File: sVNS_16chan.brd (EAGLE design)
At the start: 51 x 26.4 mm, 56 parts, among them IC2 OPA990IDCKR, IC3 EFM8SB10F8A-A-QFN24EFM8SB10F8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, J1 M50-3631042, J2 M50-3631042, J3 M50-3631042, U1 NT3H2211W0FHKH, U2 LT8410EDC-1#TRMPBF, U3 MUX36S16IRSNR, U4 MUX36S16IRSNR

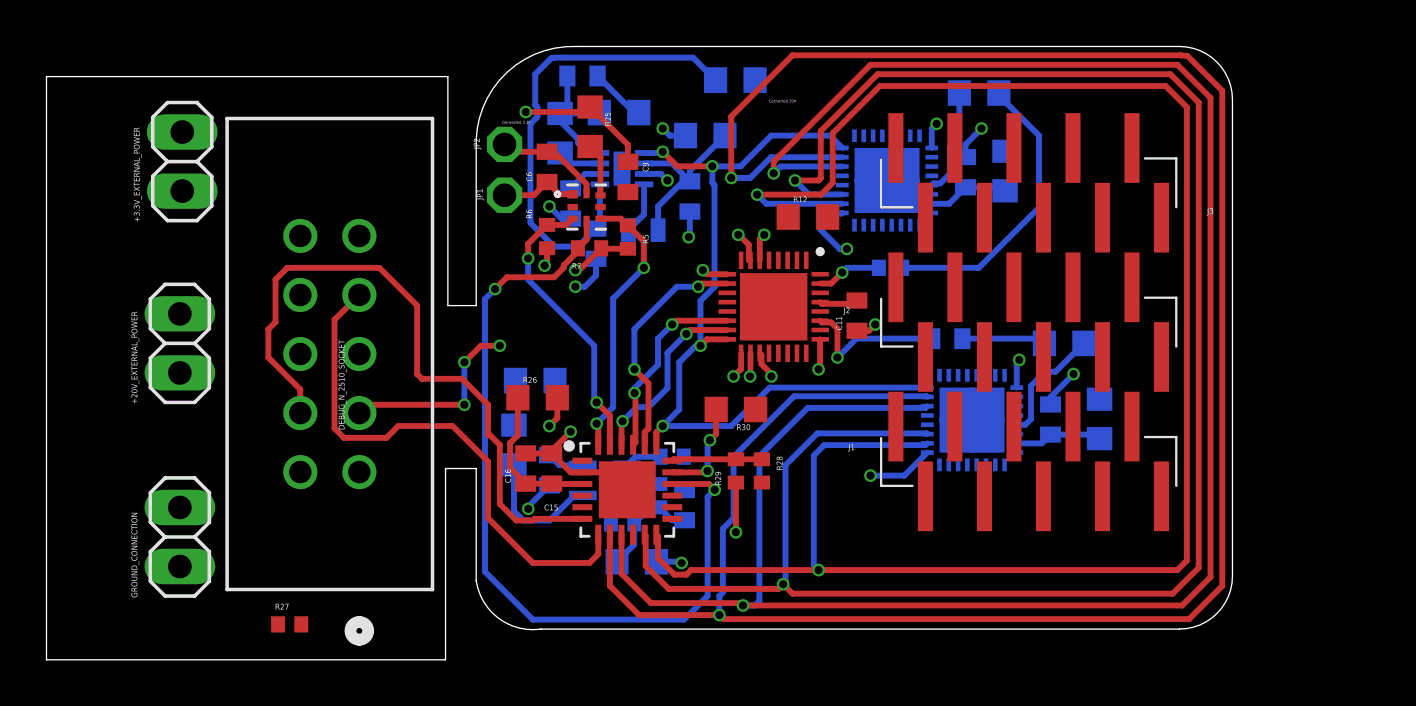
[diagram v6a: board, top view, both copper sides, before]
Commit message: Signal traces finished. Debug interface to be routed. Output stage to be mapped and routed
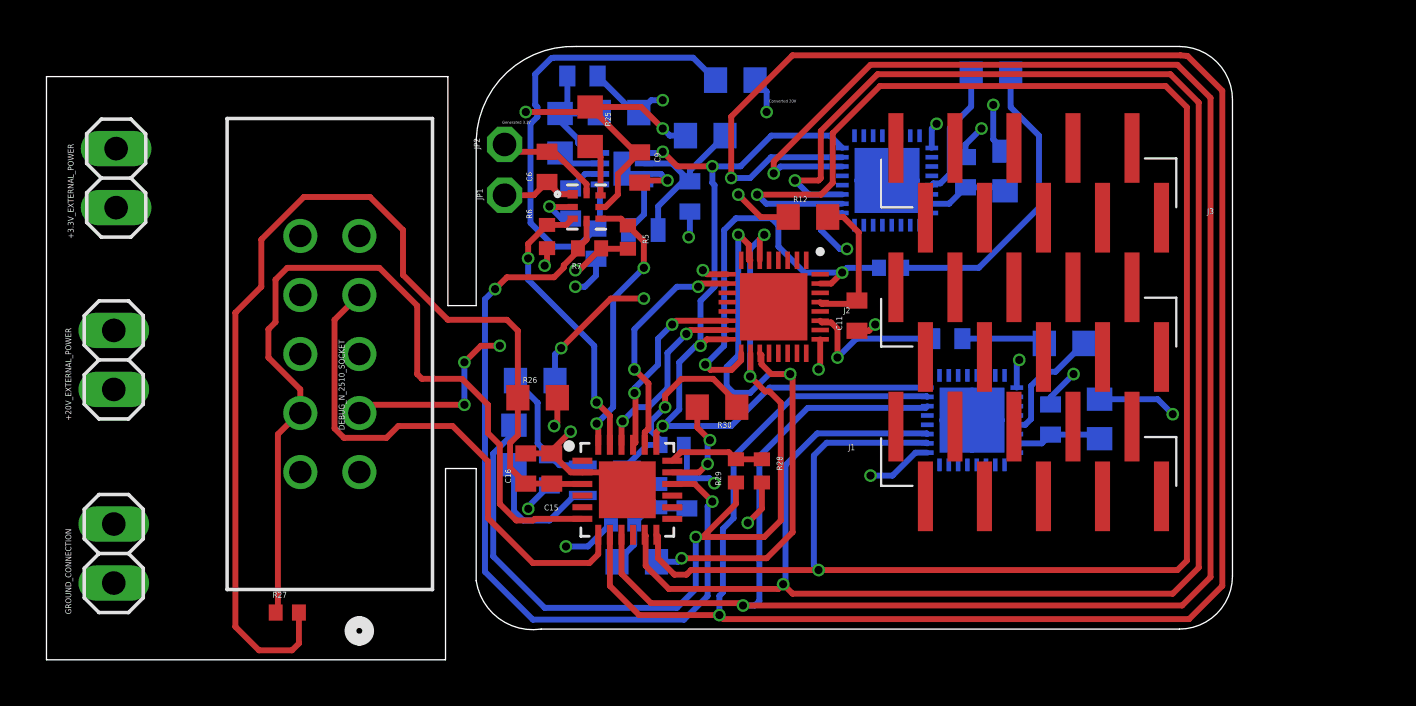
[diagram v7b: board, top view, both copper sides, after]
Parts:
- moved +20V_EXTERNAL_POWER 2.93 mm to (-16.1, 11.6)
- moved +3.3V_EXTERNAL_POWER 2.93 mm to (-16.0, 19.4)
- moved GROUND_CONNECTION 2.93 mm to (-16.1, 3.25)
- moved R14 0.96 mm to (21.6, 23.9)
- moved R30 0.82 mm to (9.86, 9.55)
- moved C9 0.65 mm to (6.53, 19.9)
- moved C13 0.52 mm to (8.56, 5.84)
- moved R27 0.52 mm to (-8.64, 0.71)
- moved R9 0.51 mm to (7.92, 7.92)
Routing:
- net +3.3V_VDD: track 6.56 -> 46.5 mm
- net I_OUT+: track 4.32 -> 40.8 mm
- net I_OUT-: track 3.66 -> 26.4 mm
- net +20V: track 0.00 -> 15.7 mm, vias 0 -> 6
- net DB: track 3.94 -> 17.8 mm
- net GND: track 41.0 -> 50.3 mm, vias 18 -> 21
- net RSTB_/_C2CK: track 28.4 -> 37.4 mm
- net +3.3V: track 11.8 -> 20.7 mm, vias 5 -> 6
- net P0.7_IREF: track 1.60 -> 8.36 mm, vias 0 -> 1
- net MUX36D08_+20V: track 1.67 -> 6.24 mm
- net OPAMP_+20V: track 1.62 -> 5.43 mm
- net BAL_B: track 4.62 -> 5.65 mm
- net BAL_B_PIN: track 12.6 -> 13.2 mm

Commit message: Output stage mapped. Ready to be routed.
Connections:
- net S10A_11: now also J1.10
- net S10B_24: now also J3.1
- net S11A_20: now also J3.9
- net S11B_18: now also J1.2
- net S12A_25: now also J2.9
- net S12B_10: now also J2.2
- net S13A_30: now also J1.9
- net S13B_5: now also J3.2
- net S15A_2: now also J3.8
- net S15B_17: now also J1.3
- net S16A_1: now also J3.10
- net S16B_19: now also J1.1
- net S1A_14: now also J1.6
- net S1B_22: now also J3.5
- net S2A_8: now also J2.6
- net S2B_27: now also J2.5
- net S3A_3: now also J3.6
- net S3B_15: now also J1.5
- net S4A_13: now also J1.7
- net S4B_4: now also J3.4
- net S5A_26: now also J2.7
- net S5B_9: now also J2.4
- net S6A_21: now also J3.7
- net S6B_16: now also J1.4
- net S7A_12: now also J1.8
- net S7B_23: now also J3.3
- net S8A_7: now also J2.8
- net S8B_28: now also J2.3
- net S9A_6: now also J2.10
- net S9B_29: now also J2.1
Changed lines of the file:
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@@
 <grid distance="4" unitdist="mil" unit="mil" style="lines" multiple="1" display="yes" altdistance="1" altunitdist="mil" altunit="mil"/>
 <layers>
-<layer number="1" name="Top" color="4" fill="1" visible="no" active="yes"/>
-<layer number="2" name="Route2(GND)" color="16" fill="1" visible="no" active="yes"/>
+<layer number="1" name="Top" color="4" fill="1" visible="yes" active="yes"/>
+<layer number="2" name="Route2(GND)" color="16" fill="1" visible="yes" active="yes"/>
 <layer number="3" name="Route3" color="17" fill="1" visible="no" active="no"/>
 <layer number="4" name="Route4" color="18" fill="1" visible="no" active="no"/>
@@
 <layer number="13" name="Route13" color="21" fill="1" visible="no" active="no"/>
 <layer number="14" name="Route14" color="22" fill="1" visible="no" active="no"/>
-<layer number="15" name="Route15(power)" color="23" fill="1" visible="no" active="yes"/>
+<layer number="15" name="Route15(power)" color="23" fill="1" visible="yes" active="yes"/>
 <layer number="16" name="Bottom" color="1" fill="1" visible="yes" active="yes"/>
 <layer number="17" name="Pads" color="2" fill="1" visible="yes" active="yes"/>
@@
 <layer number="19" name="Unrouted" color="6" fill="1" visible="yes" active="yes"/>
 <layer number="20" name="Dimension" color="24" fill="1" visible="yes" active="yes"/>
-<layer number="21" name="tPlace" color="7" fill="1" visible="no" active="yes"/>
+<layer number="21" name="tPlace" color="7" fill="1" visible="yes" active="yes"/>
 <layer number="22" name="bPlace" color="7" fill="1" visible="yes" active="yes"/>
-<layer number="23" name="tOrigins" color="15" fill="1" visible="no" active="yes"/>
+<layer number="23" name="tOrigins" color="15" fill="1" visible="yes" active="yes"/>
 <layer number="24" name="bOrigins" color="15" fill="1" visible="yes" active="yes"/>
-<layer number="25" name="tNames" color="7" fill="1" visible="no" active="yes"/>
+<layer number="25" name="tNames" color="7" fill="1" visible="yes" active="yes"/>
 <layer number="26" name="bNames" color="7" fill="1" visible="yes" active="yes"/>
 <layer number="27" name="tValues" color="7" fill="1" visible="no" active="yes"/>
@@
 <layer number="37" name="tTest" color="7" fill="1" visible="no" active="yes"/>
 <layer number="38" name="bTest" color="7" fill="1" visible="no" active="yes"/>
-<layer number="39" name="tKeepout" color="4" fill="11" visible="no" active="yes"/>
+<layer number="39" name="tKeepout" color="4" fill="11" visible="yes" active="yes"/>
 <layer number="40" name="bKeepout" color="1" fill="11" visible="yes" active="yes"/>
-<layer number="41" name="tRestrict" color="4" fill="10" visible="no" active="yes"/>
+<layer number="41" name="tRestrict" color="4" fill="10" visible="yes" active="yes"/>
 <layer number="42" name="bRestrict" color="1" fill="10" visible="yes" active="yes"/>
 <layer number="43" name="vRestrict" color="2" fill="10" visible="no" active="yes"/>
@@
 <layer number="49" name="Reference" color="7" fill="1" visible="no" active="yes"/>
 <layer number="50" name="dxf" color="7" fill="1" visible="no" active="no"/>
-<layer number="51" name="tDocu" color="7" fill="1" visible="no" active="yes"/>
+<layer number="51" name="tDocu" color="7" fill="1" visible="yes" active="yes"/>
 <layer number="52" name="bDocu" color="7" fill="1" visible="yes" active="yes"/>
 <layer number="53" name="tGND_GNDA" color="7" fill="9" visible="no" active="no"/>
@@
 <signal name="S16A_1">
 <contactref element="U3" pad="1"/>
+<contactref element="J3" pad="10"/>
+<wire x1="22.228003125" y1="7.0666" x2="28.9814" y2="17.7024" width="0" layer="19" extent="1-16"/>
 </signal>
 <signal name="S15A_2">
 <contactref element="U3" pad="2"/>
+<contactref element="J3" pad="8"/>
+<wire x1="21.828" y1="7.0666" x2="26.4414" y2="17.7024" width="0" layer="19" extent="1-16"/>
 </signal>
 <signal name="S14A">
@@
 <signal name="S13A_30">
 <contactref element="U3" pad="4"/>
+<contactref element="J1" pad="9"/>
+<wire x1="21.028003125" y1="7.0666" x2="27.7114" y2="8.7136" width="0" layer="19" extent="1-16"/>
 </signal>
 <signal name="S12A_25">
 <contactref element="U3" pad="5"/>
+<contactref element="J2" pad="9"/>
+<wire x1="20.628" y1="7.0666" x2="27.7114" y2="14.708" width="0" layer="19" extent="1-16"/>
 </signal>
 <signal name="S11A_20">
 <contactref element="U3" pad="6"/>
+<contactref element="J3" pad="9"/>
+<wire x1="20.228" y1="7.0666" x2="27.7114" y2="20.7024" width="0" layer="19" extent="1-16"/>
 </signal>
 <signal name="S10A_11">
 <contactref element="U3" pad="7"/>
+<contactref element="J1" pad="10"/>
+<wire x1="19.828003125" y1="7.0666" x2="28.9814" y2="5.7136" width="0" layer="19" extent="1-16"/>
 </signal>
 <signal name="S9A_6">
 <contactref element="U3" pad="8"/>
+<contactref element="J2" pad="10"/>
+<wire x1="19.428" y1="7.0666" x2="28.9814" y2="11.708" width="0" layer="19" extent="1-16"/>
 </signal>
 <signal name="S8A_7">
 <contactref element="U3" pad="24"/>
+<contactref element="J2" pad="8"/>
+<wire x1="22.228003125" y1="10.9166" x2="26.4414" y2="11.708" width="0" layer="19" extent="1-16"/>
 </signal>
 <signal name="S7A_12">
 <contactref element="U3" pad="23"/>
+<contactref element="J1" pad="8"/>
+<wire x1="26.4414" y1="5.7136" x2="21.828" y2="10.9166" width="0" layer="19" extent="1-16"/>
 </signal>
 <signal name="S6A_21">
 <contactref element="U3" pad="22"/>
+<contactref element="J3" pad="7"/>
+<wire x1="21.428" y1="10.9166" x2="25.1714" y2="20.7024" width="0" layer="19" extent="1-16"/>
 </signal>
 <signal name="S5A_26">
 <contactref element="U3" pad="21"/>
+<contactref element="J2" pad="7"/>
+<wire x1="21.028003125" y1="10.9166" x2="25.1714" y2="14.708" width="0" layer="19" extent="1-16"/>
 </signal>
 <signal name="S4A_13">
 <contactref element="U3" pad="20"/>
+<contactref element="J1" pad="7"/>
+<wire x1="25.1714" y1="8.7136" x2="20.628" y2="10.9166" width="0" layer="19" extent="1-16"/>
 </signal>
 <signal name="S3A_3">
 <contactref element="U3" pad="19"/>
+<contactref element="J3" pad="6"/>
+<wire x1="20.228" y1="10.9166" x2="23.9014" y2="17.7024" width="0" layer="19" extent="1-16"/>
 </signal>
 <signal name="S2A_8">
 <contactref element="U3" pad="18"/>
+<contactref element="J2" pad="6"/>
+<wire x1="19.828003125" y1="10.9166" x2="23.9014" y2="11.708" width="0" layer="19" extent="1-16"/>
 </signal>
 <signal name="S1A_14">
 <contactref element="U3" pad="17"/>
+<contactref element="J1" pad="6"/>
+<wire x1="23.9014" y1="5.7136" x2="19.428" y2="10.9166" width="0" layer="19" extent="1-16"/>
 </signal>
 <signal name="DA">
@@
 <signal name="S16B_19">
 <contactref element="U4" pad="1"/>
+<contactref element="J1" pad="1"/>
+<wire x1="17.5514" y1="8.7136" x2="18.570403125" y2="17.379" width="0" layer="19" extent="1-16"/>
 </signal>
 <signal name="S15B_17">
 <contactref element="U4" pad="2"/>
+<contactref element="J1" pad="3"/>
+<wire x1="20.0914" y1="8.7136" x2="18.1704" y2="17.379" width="0" layer="19" extent="1-16"/>
 </signal>
 <signal name="S14B">
@@
 <signal name="S13B_5">
 <contactref element="U4" pad="4"/>
+<contactref element="J3" pad="2"/>
+<wire x1="17.370403125" y1="17.379" x2="18.8214" y2="17.7024" width="0" layer="19" extent="1-16"/>
 </signal>
 <signal name="S12B_10">
 <contactref element="U4" pad="5"/>
+<contactref element="J2" pad="2"/>
+<wire x1="18.8214" y1="11.708" x2="16.9704" y2="17.379" width="0" layer="19" extent="1-16"/>
 </signal>
 <signal name="S11B_18">
 <contactref element="U4" pad="6"/>
+<contactref element="J1" pad="2"/>
+<wire x1="18.8214" y1="5.7136" x2="16.5704" y2="17.379" width="0" layer="19" extent="1-16"/>
 </signal>
 <signal name="S10B_24">
 <contactref element="U4" pad="7"/>
+<contactref element="J3" pad="1"/>
+<wire x1="16.170403125" y1="17.379" x2="17.5514" y2="20.7024" width="0" layer="19" extent="1-16"/>
 </signal>
 <signal name="S9B_29">
 <contactref element="U4" pad="8"/>
+<contactref element="J2" pad="1"/>
+<wire x1="17.5514" y1="14.708" x2="15.7704" y2="17.379" width="0" layer="19" extent="1-16"/>
 </signal>
 <signal name="S8B_28">
 <contactref element="U4" pad="24"/>
+<contactref element="J2" pad="3"/>
+<wire x1="20.0914" y1="14.708" x2="18.570403125" y2="21.229" width="0" layer="19" extent="1-16"/>
 </signal>
 <signal name="S7B_23">
 <contactref element="U4" pad="23"/>
+<contactref element="J3" pad="3"/>
+<wire x1="20.0914" y1="20.7024" x2="18.1704" y2="21.229" width="0" layer="19" extent="1-16"/>
 </signal>
 <signal name="S6B_16">
 <contactref element="U4" pad="22"/>
+<contactref element="J1" pad="4"/>
+<wire x1="21.3614" y1="5.7136" x2="17.7704" y2="21.229" width="0" layer="19" extent="1-16"/>
 </signal>
 <signal name="S5B_9">
 <contactref element="U4" pad="21"/>
+<contactref element="J2" pad="4"/>
+<wire x1="21.3614" y1="11.708" x2="17.370403125" y2="21.229" width="0" layer="19" extent="1-16"/>
 </signal>
 <signal name="S4B_4">
 <contactref element="U4" pad="20"/>
+<contactref element="J3" pad="4"/>
+<wire x1="21.3614" y1="17.7024" x2="16.9704" y2="21.229" width="0" layer="19" extent="1-16"/>
 </signal>
 <signal name="S3B_15">
 <contactref element="U4" pad="19"/>
+<contactref element="J1" pad="5"/>
+<wire x1="22.6314" y1="8.7136" x2="16.5704" y2="21.229" width="0" layer="19" extent="1-16"/>
 </signal>
 <signal name="S2B_27">
 <contactref element="U4" pad="18"/>
+<contactref element="J2" pad="5"/>
+<wire x1="22.6314" y1="14.708" x2="16.170403125" y2="21.229" width="0" layer="19" extent="1-16"/>
 </signal>
 <signal name="S1B_22">
 <contactref element="U4" pad="17"/>
+<contactref element="J3" pad="5"/>
+<wire x1="15.7704" y1="21.229" x2="22.6314" y2="20.7024" width="0" layer="19" extent="1-16"/>
 </signal>
 <signal name="I_OUT-">
